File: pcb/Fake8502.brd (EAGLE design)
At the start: 69.8 x 21 mm, 16 parts, among them IC2 XC9572XLTQG100, IC5 HDR, IC6 65(C)02

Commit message: Fixed port definitions
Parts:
- removed IC5: HDR, commodore:DIL40-ROUNDPAD
- added IC3: XC9572XLTQG100, xilinx_xc95XXXxl:TQFP100
- added SJ1: (no value), jumper:SJ
- IC1: value 65(C)02 -> W65C02SP
- IC2: value XC9572XLTQG100 -> MOS8502; device xilinx_xc95XXXxl:TQFP100 -> commodore:DIL40-ROUNDPAD
- moved IC2 34.3 mm to (44.5, 11.4), flipped to the top
- renumbered IC6 to IC1
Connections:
- removed net !RDY': IC1.2, IC2.29
- new net N$1: IC1.1, SJ1.2
- net !IRQ: now also IC2.3, IC3.30; no longer IC2.30, IC5.3
- net !NMI: now also IC2.4, IC3.32; no longer IC2.32, IC5.4
- net !RDY: now also IC1.2, IC2.2, IC3.28; no longer IC2.28, IC5.2
- net !RESET: now also IC2.40, IC3.99; no longer IC2.99, IC5.40
- net +3V3: now also IC3.26, IC3.38, IC3.5, IC3.51, IC3.57, IC3.88, IC3.98; no longer IC2.26, IC2.38, IC2.5, IC2.51, IC2.57, IC2.88, IC2.98
- net A'0: now also IC3.20; no longer IC2.20
- net A'1: now also IC3.17; no longer IC2.17
- net A'10: now also IC3.56; no longer IC2.56
- net A'11: now also IC3.59; no longer IC2.59
- net A'12: now also IC3.71; no longer IC2.71
- net A'13: now also IC3.74; no longer IC2.74
- net A'14: now also IC3.77; no longer IC2.77
- net A'15: now also IC3.79; no longer IC2.79
- net A'2: now also IC3.15; no longer IC2.15
- net A'3: now also IC3.33; no longer IC2.33
- net A'4: now also IC3.36; no longer IC2.36
- net A'5: now also IC3.39; no longer IC2.39
- net A'6: now also IC3.41; no longer IC2.41
- net A'7: now also IC3.49; no longer IC2.49
- net A'8: now also IC3.52; no longer IC2.52
- net A'9: now also IC3.54; no longer IC2.54
- net A0: now also IC2.7, IC3.23; no longer IC2.23, IC5.7
- net A1: now also IC2.8, IC3.22; no longer IC2.22, IC5.8
- net A10: now also IC2.17, IC3.53; no longer IC2.53, IC5.17
- net A11: now also IC2.18, IC3.55; no longer IC2.55, IC5.18
- net A12: now also IC2.19, IC3.58; no longer IC2.58, IC5.19
- net A13: now also IC2.20, IC3.60; no longer IC2.60, IC5.20
- net A14: now also IC2.22, IC3.72; no longer IC2.72, IC5.22
- net A15: now also IC2.23, IC3.76; no longer IC2.76, IC5.23
- net A2: now also IC2.9, IC3.18; no longer IC2.18, IC5.9
- net A3: now also IC2.10, IC3.16; no longer IC2.16, IC5.10
- net A4: now also IC2.11, IC3.14; no longer IC2.14, IC5.11
- net A5: now also IC2.12, IC3.35; no longer IC2.35, IC5.12
- net A6: now also IC2.13, IC3.37; no longer IC2.37, IC5.13
- net A7: now also IC2.14, IC3.40; no longer IC2.40, IC5.14
- net A8: now also IC2.15, IC3.42; no longer IC2.42, IC5.15
- net A9: now also IC2.16, IC3.50; no longer IC2.50, IC5.16
- net AEC: now also IC2.5, IC3.25; no longer IC2.25, IC5.5
- net D'0: now also IC3.8; no longer IC2.8
- net D'1: now also IC3.10; no longer IC2.10
- net D'2: now also IC3.12; no longer IC2.12
- net D'3: now also IC3.93; no longer IC2.93
- net D'4: now also IC3.91; no longer IC2.91
- net D'5: now also IC3.89; no longer IC2.89
- net D'6: now also IC3.86; no longer IC2.86
- net D'7: now also IC3.82; no longer IC2.82
- net D0: now also IC2.38, IC3.96; no longer IC2.96, IC5.38
- net D1: now also IC2.37, IC3.95; no longer IC2.95, IC5.37
- net D2: now also IC2.36, IC3.94; no longer IC2.94, IC5.36
- net D3: now also IC2.35, IC3.1; no longer IC2.1, IC5.35
- net D4: now also IC2.34, IC3.3; no longer IC2.3, IC5.34
- net D5: now also IC2.33, IC3.6; no longer IC2.6, IC5.33
- net D6: now also IC2.32, IC3.9; no longer IC2.9, IC5.32
- net D7: now also IC2.31, IC3.11; no longer IC2.11, IC5.31
- net GND: now also IC3.100, IC3.21, IC3.31, IC3.44, IC3.62, IC3.69, IC3.75, IC3.84, SJ1.1; no longer IC1.1, IC2.100, IC2.31, IC2.44, IC2.62, IC2.69, IC2.75, IC2.84, IC5.21
- net N$3: now also IC3.48; no longer IC2.48
- net N$4: now also IC3.47; no longer IC2.47
- net N$5: now also IC3.45; no longer IC2.45
- net N$6: now also IC3.83; no longer IC2.83
- net P0: now also IC2.30, IC3.13; no longer IC2.13, IC5.30
- net P1: now also IC2.29, IC3.92; no longer IC2.92, IC5.29
- net P2: now also IC2.28, IC3.90; no longer IC2.90, IC5.28
- net P3: now also IC2.27, IC3.87; no longer IC2.87, IC5.27
- net P4: now also IC2.26, IC3.85; no longer IC2.85, IC5.26
- net P5: now also IC2.25, IC3.81; no longer IC2.81, IC5.25
- net P6: now also IC2.24, IC3.78; no longer IC2.78, IC5.24
- net PHI: now also IC2.1, IC3.27; no longer IC2.27, IC5.1
- net R/!W: now also IC2.39, IC3.97; no longer IC2.97, IC5.39
- net R/!W': now also IC3.4; no longer IC2.4
- net VCC: now also IC2.6; no longer IC5.6
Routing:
- net !RDY': track 9.69 -> 0.00 mm
- net !RDY: track 9.73 -> 11.2 mm

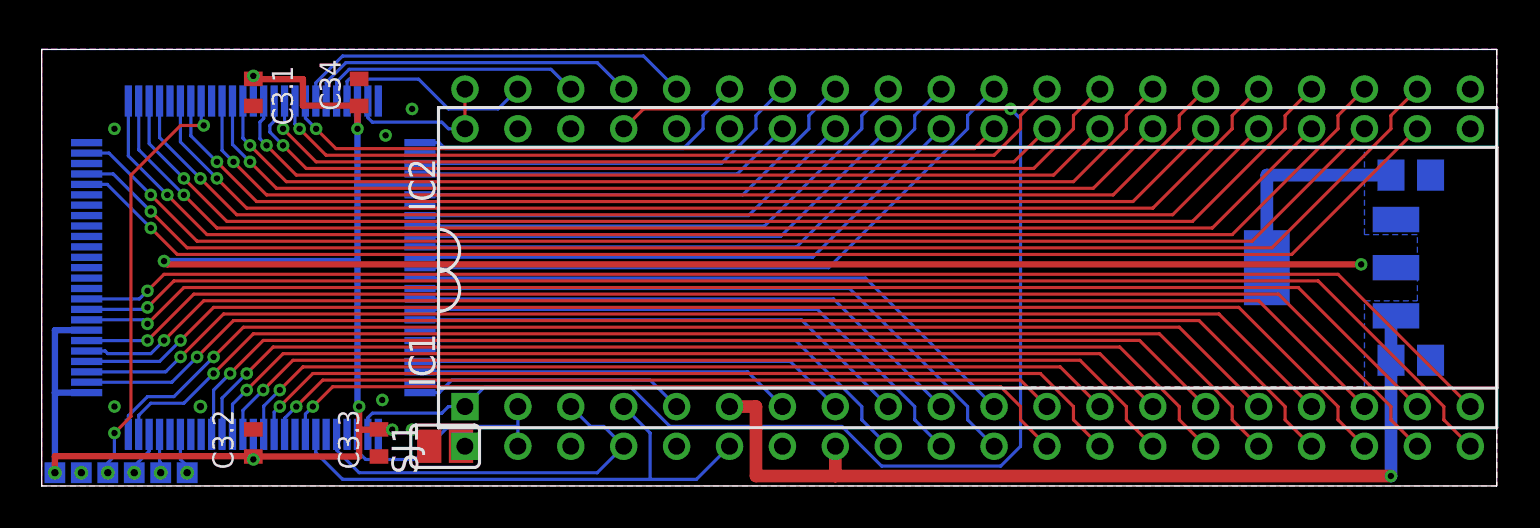
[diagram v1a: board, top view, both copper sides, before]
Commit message: Created GFX for schematic and PCB
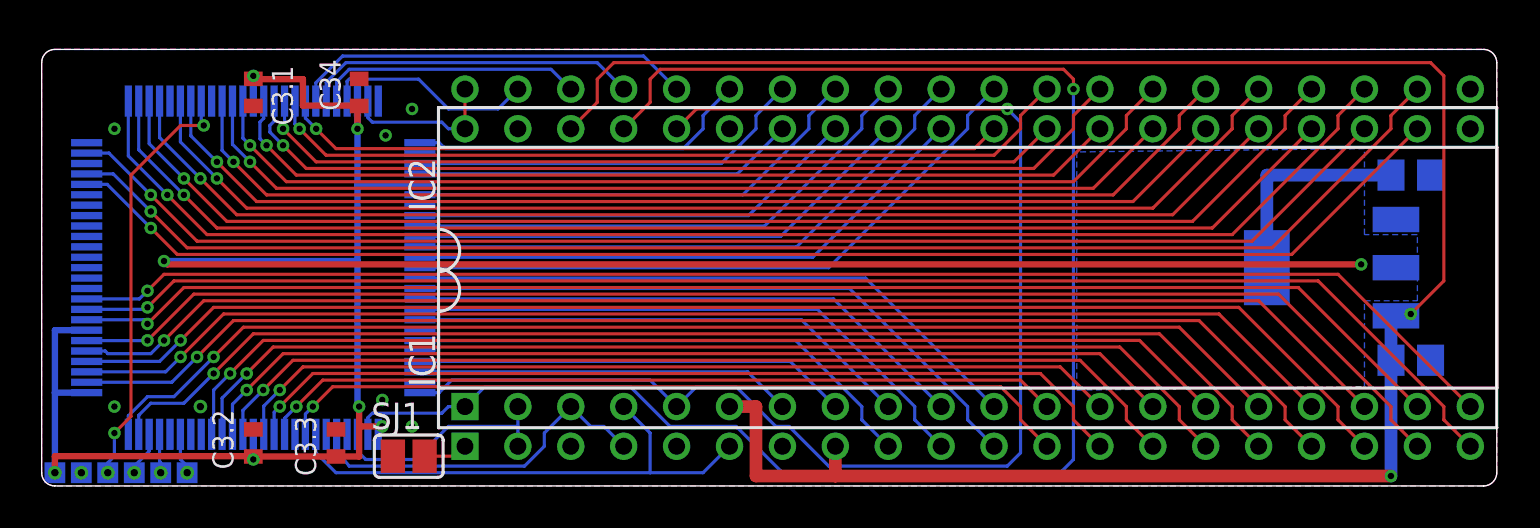
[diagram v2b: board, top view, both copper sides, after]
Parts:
- moved C3.3 2.06 mm to (14.1, 2.06), turned to 90 degrees
- moved SJ1 1.81 mm to (17.6, 1.43)
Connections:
- net AEC: now also IC1.36
- net VCC: now also IC1.38
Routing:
- net VCC: track 44.4 -> 101.4 mm, vias 1 -> 2
- net AEC: track 13.1 -> 64.9 mm, vias 0 -> 1
- net PHI: track 70.1 -> 79.1 mm
- net N$1: track 0.00 -> 2.13 mm
- net !IRQ: track 18.8 -> 17.3 mm
- net +3V3: track 135.7 -> 134.8 mm
- net !NMI: track 25.9 -> 25.4 mm
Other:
- outline, holes or cut-outs redrawn
